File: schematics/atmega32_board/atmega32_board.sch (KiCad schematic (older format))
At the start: 1 part

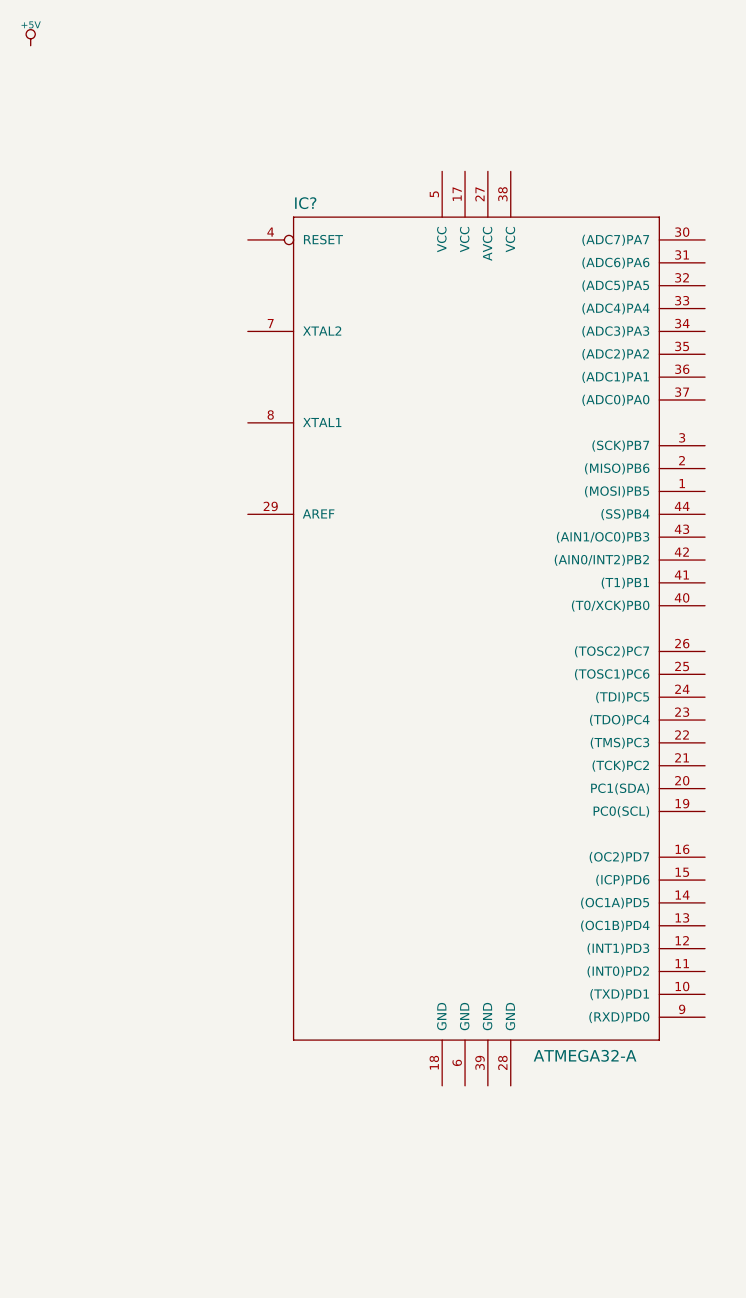
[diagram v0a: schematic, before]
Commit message: Changes:	sync with my avr_sdk
		NOTE: still not useable !
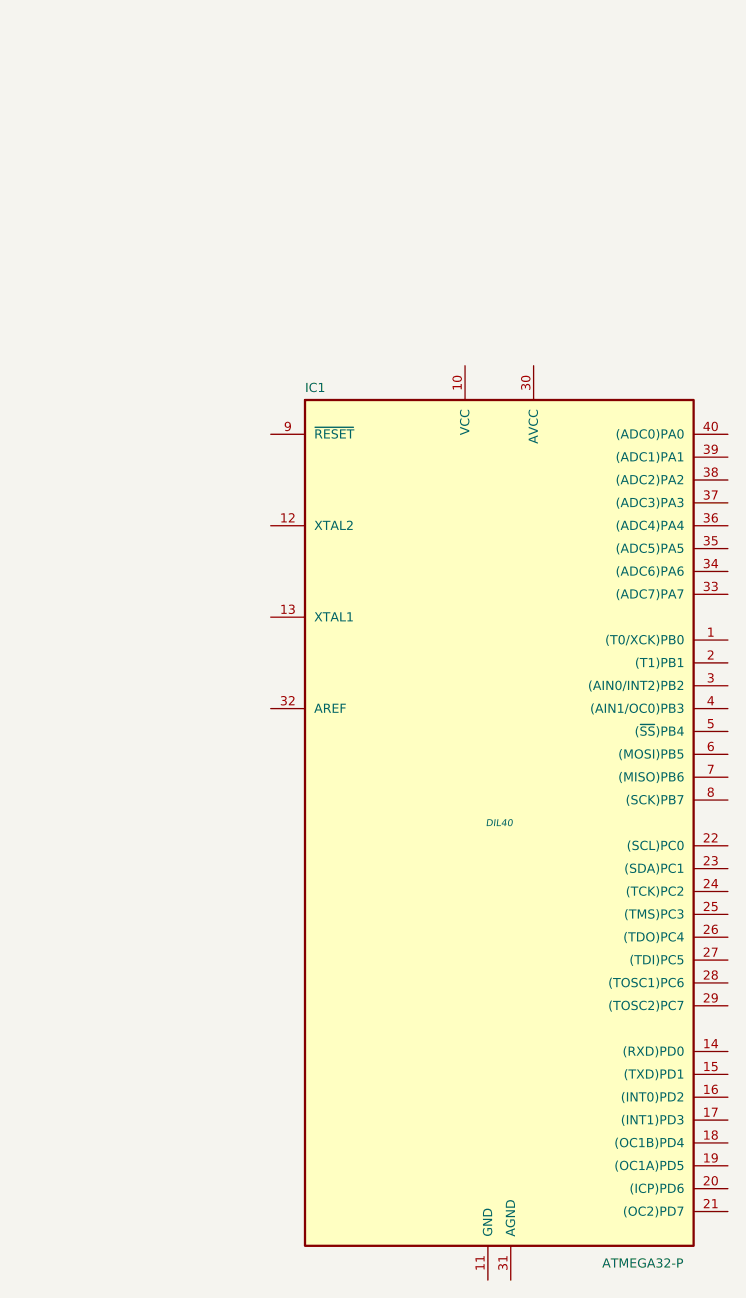
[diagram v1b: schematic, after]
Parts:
- removed IC?: ATMEGA32-A, TQFP44, symbol ATMEGA32-A
- added IC1: ATMEGA32-P, DIL40, symbol ATMEGA32-P
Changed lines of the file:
@@
-EESchema Schematic File Version 2  date Di 22 Jul 2014 16:01:04 CEST
+EESchema Schematic File Version 2
 LIBS:power
 LIBS:device
@@
 LIBS:valves
 LIBS:atmega32_board-cache
-EELAYER 25  0
+EELAYER 27 0
 EELAYER END
-$Descr A4 11700 8267
+$Descr A4 11693 8268
 encoding utf-8
 Sheet 1 1
 Title ""
-Date "22 jul 2014"
+Date "23 jul 2014"
 Rev ""
 Comp ""
@@
 $EndDescr
 $Comp
-L +5V #PWR?
-U 1 1 53CE6E84
-P 900 1300
-F 0 "#PWR?" H 900 1390 20  0001 C CNN
-F 1 "+5V" H 900 1390 30  0000 C CNN
-	1    900  1300
+L ATMEGA32-P IC1
+U 1 1 53CF7D74
+P 2950 4700
+F 0 "IC1" H 2100 6580 40  0000 L BNN
+F 1 "ATMEGA32-P" H 3400 2750 40  0000 L BNN
+F 2 "DIL40" H 2950 4700 30  0000 C CIN
+F 3 "" H 2950 4700 60  0000 C CNN
+	1    2950 4700
 	1    0    0    -1
 $EndComp
-$Comp
-L ATMEGA32-A IC?
-U 1 1 53CE6CE8
-P 2850 3850
-F 0 "IC?" H 2050 5680 50  0000 L BNN
-F 1 "ATMEGA32-A" H 3100 1950 50  0000 L BNN
-F 2 "TQFP44" H 3350 1875 50  0001 C CNN
-	1    2850 3850
-	1    0    0    -1
-$EndComp
